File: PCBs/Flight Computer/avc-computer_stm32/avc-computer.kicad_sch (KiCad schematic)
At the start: 1 part, among them J5 ESC Connector

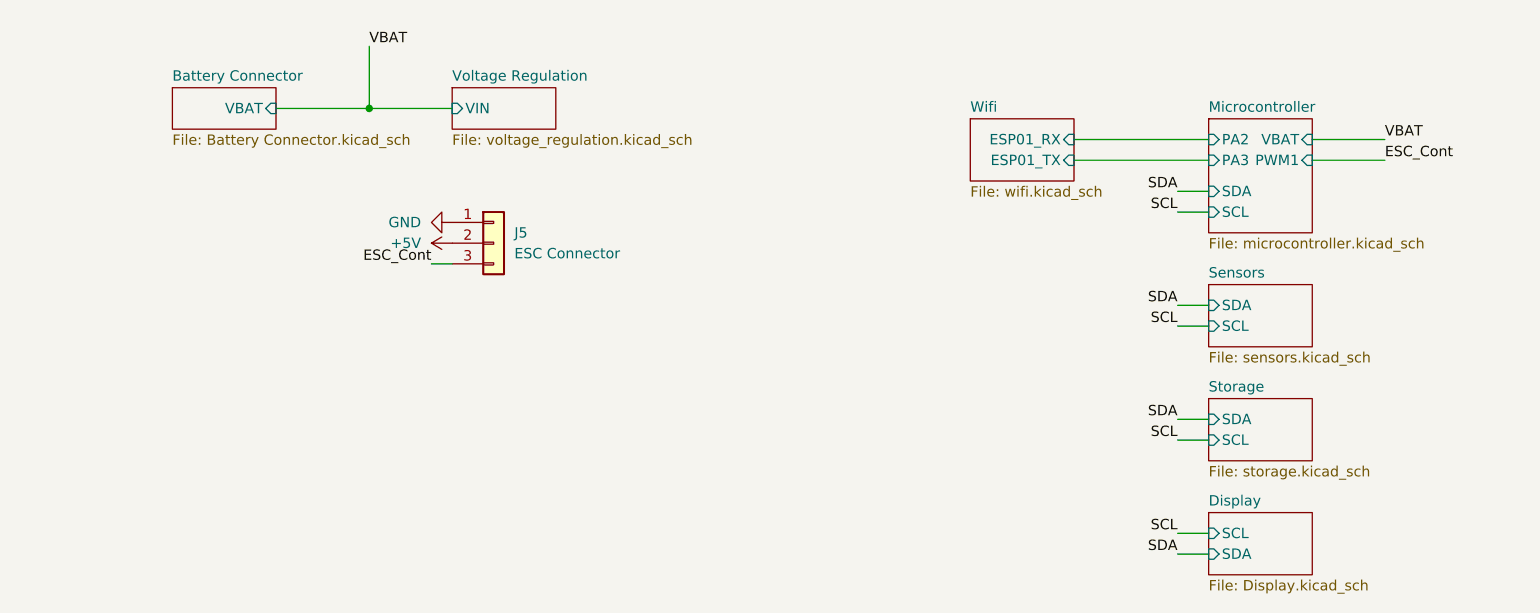
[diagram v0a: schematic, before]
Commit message: Began fixing reference designators
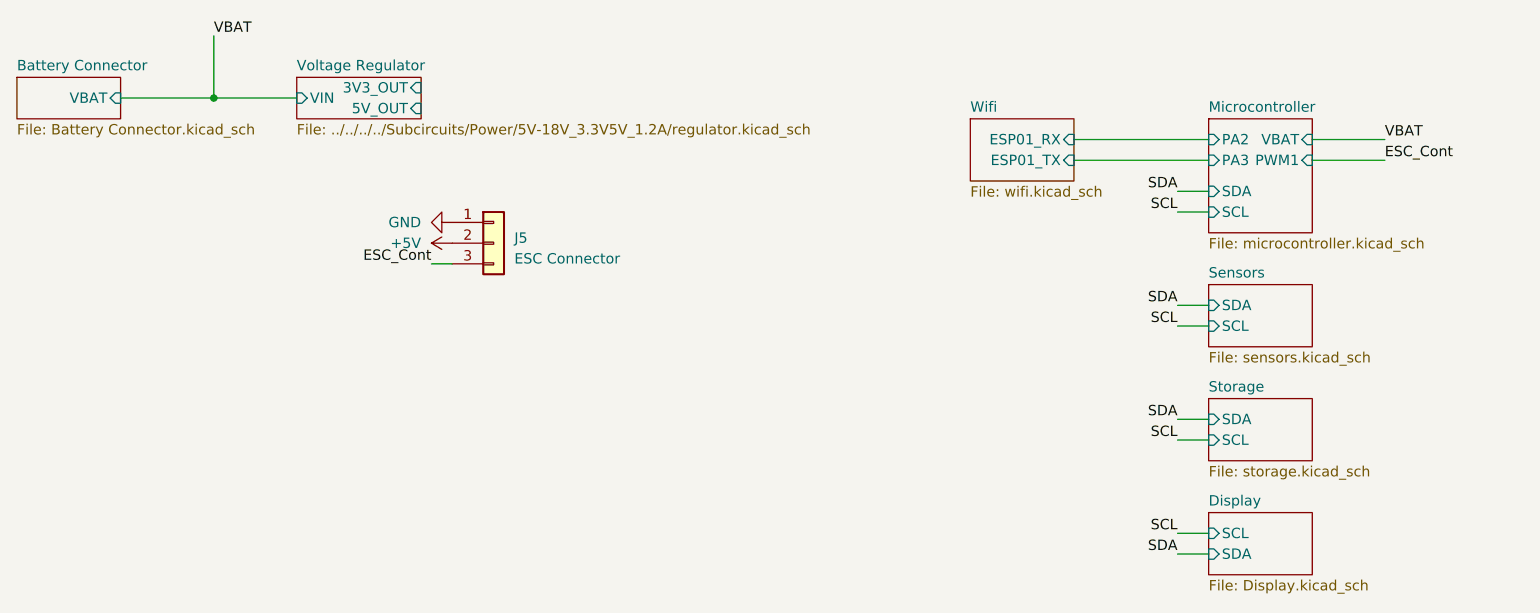
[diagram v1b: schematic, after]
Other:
- removed sheet Voltage Regulation
- added sheet Voltage Regulator (../../../../Subcircuits/Power/5V-18V_3.3V5V_1.2A/regulator.kicad_sch)
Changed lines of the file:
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@@
 (kicad_sch (version 20230121) (generator eeschema)
   (paper "A4")
-  (junction (at 92.71 68.58) (diameter 0) (color 0 0 0 0)
+  (junction (at 73.66 67.31) (diameter 0) (color 0 0 0 0)
   )
   (wire (pts (xy 191.77 106.68) (xy 195.58 106.68))
     (stroke (width 0) (type default))
   )
-  (wire (pts (xy 92.71 60.96) (xy 92.71 68.58))
+  (wire (pts (xy 73.66 59.69) (xy 73.66 67.31))
     (stroke (width 0) (type default))
   )
@@
     (stroke (width 0) (type default))
   )
+  (wire (pts (xy 73.66 67.31) (xy 83.82 67.31))
+    (stroke (width 0) (type default))
+  )
   (wire (pts (xy 191.77 81.28) (xy 195.58 81.28))
     (stroke (width 0) (type default))
@@
     (stroke (width 0) (type default))
   )
-  (wire (pts (xy 81.28 68.58) (xy 92.71 68.58))
+  (wire (pts (xy 62.23 67.31) (xy 73.66 67.31))
     (stroke (width 0) (type default))
   )
@@
   )
   (wire (pts (xy 195.58 123.19) (xy 191.77 123.19))
-    (stroke (width 0) (type default))
-  )
-  (wire (pts (xy 92.71 68.58) (xy 102.87 68.58))
     (stroke (width 0) (type default))
   )
@@
     (effects (font (size 1.27 1.27)) (justify right bottom))
   )
-  (label "VBAT" (at 92.71 60.96 0) (fields_autoplaced)
+  (label "VBAT" (at 73.66 59.69 0) (fields_autoplaced)
     (effects (font (size 1.27 1.27)) (justify left bottom))
   )
@@
   (symbol (lib_id "power:GND") (at 102.87 82.55 270) (unit 1)
     (in_bom yes) (on_board yes) (dnp no) (fields_autoplaced)
-    (property "Reference" "#PWR0160" (at 96.52 82.55 0)
+    (property "Reference" "#PWR01" (at 96.52 82.55 0)
       (effects (font (size 1.27 1.27)) hide)
     )
@@
       (project "avc-computer"
         (path "/e63e39d7-6ac0-4ffd-8aa3-1841a4541b55"
-          (reference "#PWR0160") (unit 1)
+          (reference "#PWR01") (unit 1)
         )
       )
@@
   (symbol (lib_id "power:+5V") (at 102.87 85.09 90) (unit 1)
     (in_bom yes) (on_board yes) (dnp no) (fields_autoplaced)
-    (property "Reference" "#PWR0161" (at 106.68 85.09 0)
+    (property "Reference" "#PWR02" (at 106.68 85.09 0)
       (effects (font (size 1.27 1.27)) hide)
     )
@@
       (project "avc-computer"
         (path "/e63e39d7-6ac0-4ffd-8aa3-1841a4541b55"
-          (reference "#PWR0161") (unit 1)
+          (reference "#PWR02") (unit 1)
         )
       )
@@
   (symbol (lib_id "Connector_Generic:Conn_01x03") (at 107.95 85.09 0) (unit 1)
     (in_bom yes) (on_board yes) (dnp no) (fields_autoplaced)
-    (property "Reference" "J5" (at 110.49 83.8199 0)
-      (effects (font (size 1.27 1.27)) (justify left))
-    )
-    (property "Value" "ESC Connector" (at 110.49 86.3599 0)
+    (property "Reference" "J5" (at 110.49 84.455 0)
+      (effects (font (size 1.27 1.27)) (justify left))
+    )
+    (property "Value" "ESC Connector" (at 110.49 86.995 0)
       (effects (font (size 1.27 1.27)) (justify left))
     )
@@
     )
   )
-  (sheet (at 102.87 66.04) (size 12.7 5.08) (fields_autoplaced)
-    (stroke (width 0.1524) (type solid))
-    (fill (color 0 0 0 0.0000))
-    (property "Sheetname" "Voltage Regulation" (at 102.87 65.3284 0)
-      (effects (font (size 1.27 1.27)) (justify left bottom))
-    )
-    (property "Sheetfile" "voltage_regulation.kicad_sch" (at 102.87 71.7046 0)
-      (effects (font (size 1.27 1.27)) (justify left top))
-    )
-    (pin "VIN" input (at 102.87 68.58 180)
-      (effects (font (size 1.27 1.27)) (justify left))
-    )
-    (instances
-      (project "avc-computer"
-        (path "/e63e39d7-6ac0-4ffd-8aa3-1841a4541b55" (page "7"))
-      )
-    )
-  )
   (sheet (at 195.58 118.11) (size 12.7 7.62) (fields_autoplaced)
     (stroke (width 0.1524) (type solid))
@@
     )
   )
-  (sheet (at 68.58 66.04) (size 12.7 5.08) (fields_autoplaced)
-    (stroke (width 0.1524) (type solid))
-    (fill (color 0 0 0 0.0000))
-    (property "Sheetname" "Battery Connector" (at 68.58 65.3284 0)
-      (effects (font (size 1.27 1.27)) (justify left bottom))
-    )
-    (property "Sheetfile" "Battery Connector.kicad_sch" (at 68.58 71.7046 0)
-      (effects (font (size 1.27 1.27)) (justify left top))
-    )
-    (pin "VBAT" input (at 81.28 68.58 0)
-      (effects (font (size 1.27 1.27)) (justify right))
-    )
+  (sheet (at 83.82 64.77) (size 15.24 5.08) (fields_autoplaced)
+    (stroke (width 0.1524) (type solid))
+    (fill (color 0 0 0 0.0000))
+    (property "Sheetname" "Voltage Regulator" (at 83.82 64.0584 0)
+      (effects (font (size 1.27 1.27)) (justify left bottom))
+    )
+    (property "Sheetfile" "../../../../Subcircuits/Power/5V-18V_3.3V5V_1.2A/regulator.kicad_sch" (at 83.82 70.4346 0)
+      (effects (font (size 1.27 1.27)) (justify left top))
+    )
+    (pin "3V3_OUT" input (at 99.06 66.04 0)
+      (effects (font (size 1.27 1.27)) (justify right))
+    )
+    (pin "5V_OUT" input (at 99.06 68.58 0)
+      (effects (font (size 1.27 1.27)) (justify right))
+    )
+    (pin "VIN" input (at 83.82 67.31 180)
+      (effects (font (size 1.27 1.27)) (justify left))
+    )
+    (instances
+      (project "avc-computer"
+        (path "/e63e39d7-6ac0-4ffd-8aa3-1841a4541b55" (page "9"))
+      )
+    )
+  )
+  (sheet (at 49.53 64.77) (size 12.7 5.08) (fields_autoplaced)
+    (stroke (width 0.1524) (type solid))
+    (fill (color 0 0 0 0.0000))
+    (property "Sheetname" "Battery Connector" (at 49.53 64.0584 0)
+      (effects (font (size 1.27 1.27)) (justify left bottom))
+    )
+    (property "Sheetfile" "Battery Connector.kicad_sch" (at 49.53 70.4346 0)
+      (effects (font (size 1.27 1.27)) (justify left top))
+    )
+    (pin "VBAT" input (at 62.23 67.31 0)
+      (effects (font (size 1.27 1.27)) (justify right))
+    )

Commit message: Relpaced swithcing regulator with linear regulator. Removed unneccesary components. Replaced barometric pressure sensor with better one. Added connectors for brake servo & hall effect sensor
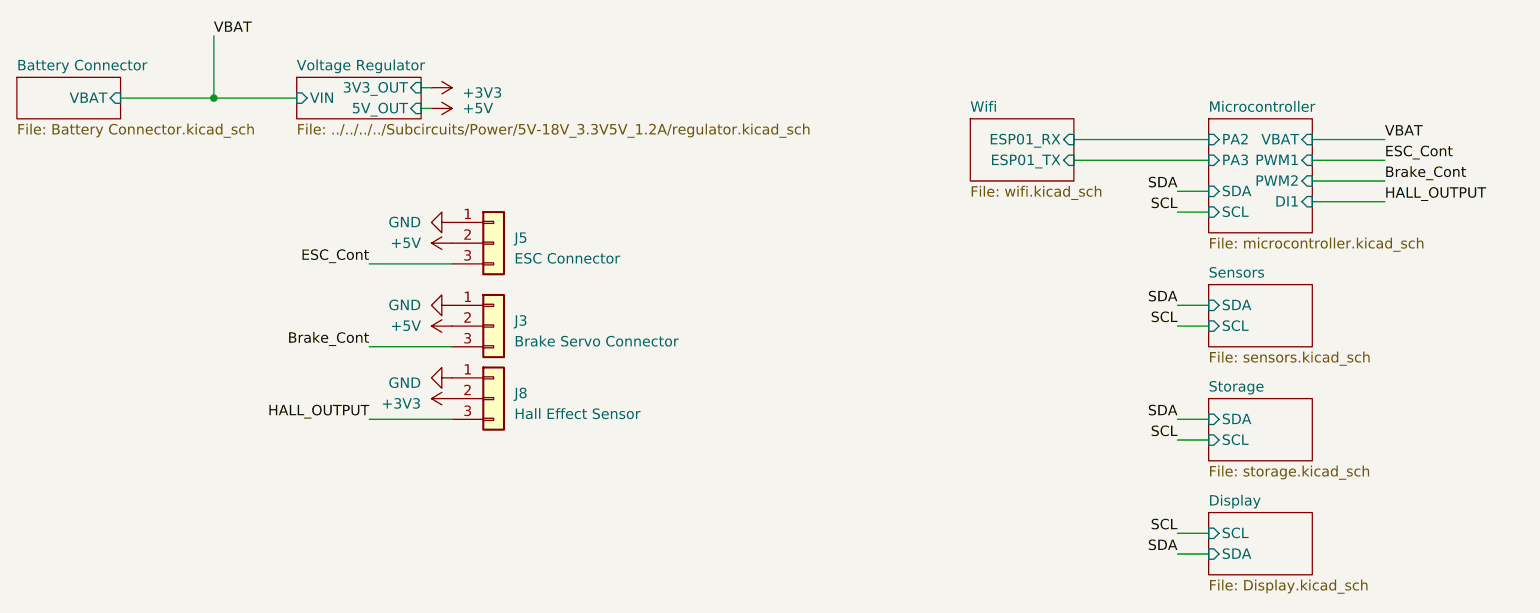
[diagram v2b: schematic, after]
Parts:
- added J3: Brake Servo Connector, Connector_PinHeader_2.54mm:PinHeader_1x03_P2.54mm_Vertical, symbol Connector_Generic:Conn_01x03
- added J8: Hall Effect Sensor, Connector_PinHeader_2.54mm:PinHeader_1x03_P2.54mm_Vertical, symbol Connector_Generic:Conn_01x03
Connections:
- net +5V: now also J3.2 (Pin_2)
- net GND: now also J3.1 (Pin_1), J8.1 (Pin_1)
- new net +3V3: J8.2 (Pin_2)
- new net Brake_Cont: J3.3 (Pin_3)
- new net HALL_OUTPUT: J8.3 (Pin_3)
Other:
- sheet Microcontroller ports: added DI1, PWM2; removed none

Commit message: Replaced IMU and added 1.9v bus
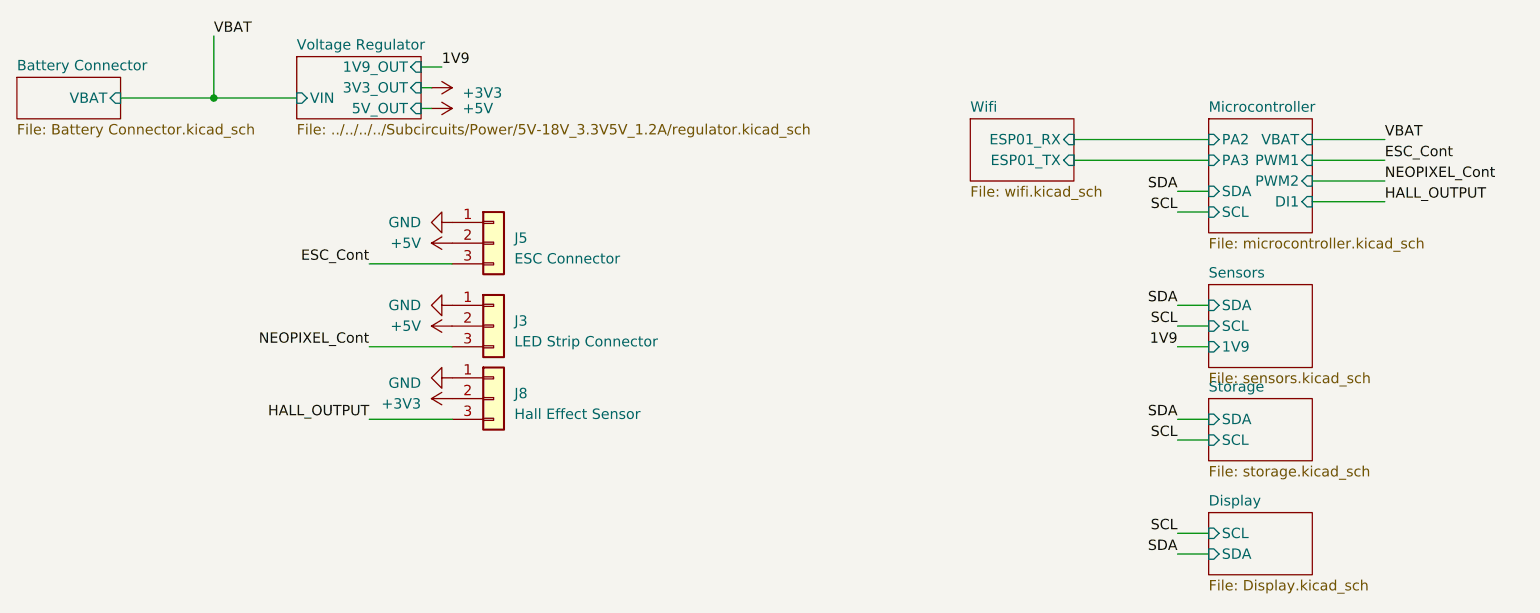
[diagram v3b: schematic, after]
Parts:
- J3: value Brake Servo Connector -> LED Strip Connector
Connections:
- net Brake_Cont renamed NEOPIXEL_Cont
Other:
- sheet Sensors ports: added 1V9; removed none
- sheet Voltage Regulator ports: added 1V9_OUT; removed none
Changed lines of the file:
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@@
   (junction (at 73.66 67.31) (diameter 0) (color 0 0 0 0)
   )
+  (wire (pts (xy 99.06 63.5) (xy 101.6 63.5))
+    (stroke (width 0) (type default))
+  )
   (wire (pts (xy 191.77 106.68) (xy 195.58 106.68))
     (stroke (width 0) (type default))
@@
     (stroke (width 0) (type default))
   )
+  (wire (pts (xy 191.77 97.79) (xy 195.58 97.79))
+    (stroke (width 0) (type default))
+  )
   (wire (pts (xy 62.23 67.31) (xy 73.66 67.31))
     (stroke (width 0) (type default))
@@
     (stroke (width 0) (type default))
   )
-  (label "Brake_Cont" (at 217.17 77.47 0) (fields_autoplaced)
+  (label "NEOPIXEL_Cont" (at 217.17 77.47 0) (fields_autoplaced)
     (effects (font (size 1.27 1.27)) (justify left bottom))
   )
@@
     (effects (font (size 1.27 1.27)) (justify left bottom))
   )
+  (label "1V9" (at 101.6 63.5 0) (fields_autoplaced)
+    (effects (font (size 1.27 1.27)) (justify left bottom))
+  )
   (label "SCL" (at 191.77 95.25 180) (fields_autoplaced)
     (effects (font (size 1.27 1.27)) (justify right bottom))
@@
     (effects (font (size 1.27 1.27)) (justify right bottom))
   )
+  (label "1V9" (at 191.77 97.79 180) (fields_autoplaced)
+    (effects (font (size 1.27 1.27)) (justify right bottom))
+  )
   (label "SDA" (at 191.77 106.68 180) (fields_autoplaced)
     (effects (font (size 1.27 1.27)) (justify right bottom))
@@
     (effects (font (size 1.27 1.27)) (justify right bottom))
   )
-  (label "Brake_Cont" (at 92.71 97.79 180) (fields_autoplaced)
+  (label "NEOPIXEL_Cont" (at 92.71 97.79 180) (fields_autoplaced)
     (effects (font (size 1.27 1.27)) (justify right bottom))
   )
@@
       (effects (font (size 1.27 1.27)) (justify left))
     )
-    (property "Value" "Brake Servo Connector" (at 110.49 97.155 0)
+    (property "Value" "LED Strip Connector" (at 110.49 97.155 0)
       (effects (font (size 1.27 1.27)) (justify left))
     )
@@
     )
   )
-  (sheet (at 195.58 90.17) (size 12.7 7.62) (fields_autoplaced)
+  (sheet (at 195.58 90.17) (size 12.7 10.16) (fields_autoplaced)
     (stroke (width 0.1524) (type solid))
     (fill (color 0 0 0 0.0000))
@@
       (effects (font (size 1.27 1.27)) (justify left bottom))
     )
-    (property "Sheetfile" "sensors.kicad_sch" (at 195.58 98.3746 0)
+    (property "Sheetfile" "sensors.kicad_sch" (at 195.58 100.9146 0)
       (effects (font (size 1.27 1.27)) (justify left top))
     )
@@
     )
     (pin "SCL" input (at 195.58 95.25 180)
+      (effects (font (size 1.27 1.27)) (justify left))
+    )
+    (pin "1V9" input (at 195.58 97.79 180)
       (effects (font (size 1.27 1.27)) (justify left))
     )
@@
     )
   )
-  (sheet (at 83.82 64.77) (size 15.24 5.08) (fields_autoplaced)
+  (sheet (at 83.82 62.23) (size 15.24 7.62) (fields_autoplaced)
     (stroke (width 0.1524) (type solid))
     (fill (color 0 0 0 0.0000))
-    (property "Sheetname" "Voltage Regulator" (at 83.82 64.0584 0)
+    (property "Sheetname" "Voltage Regulator" (at 83.82 61.5184 0)
       (effects (font (size 1.27 1.27)) (justify left bottom))
     )
@@
       (effects (font (size 1.27 1.27)) (justify left))
     )
-    (instances
+    (pin "1V9_OUT" input (at 99.06 63.5 0)
+      (effects (font (size 1.27 1.27)) (justify right))
+    )
+    (instances
